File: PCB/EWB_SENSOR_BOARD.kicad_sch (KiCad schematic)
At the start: 31 parts, among them J3 B4B-PH-K-S, J4 Conn_01x06_Pin, U1 ESP32-C3-WROOM-02-N4, U2 AZ1117CD-3.3TRG1, U3 AP64500SP-13, Y1 ABS07-32.768KHZ-T

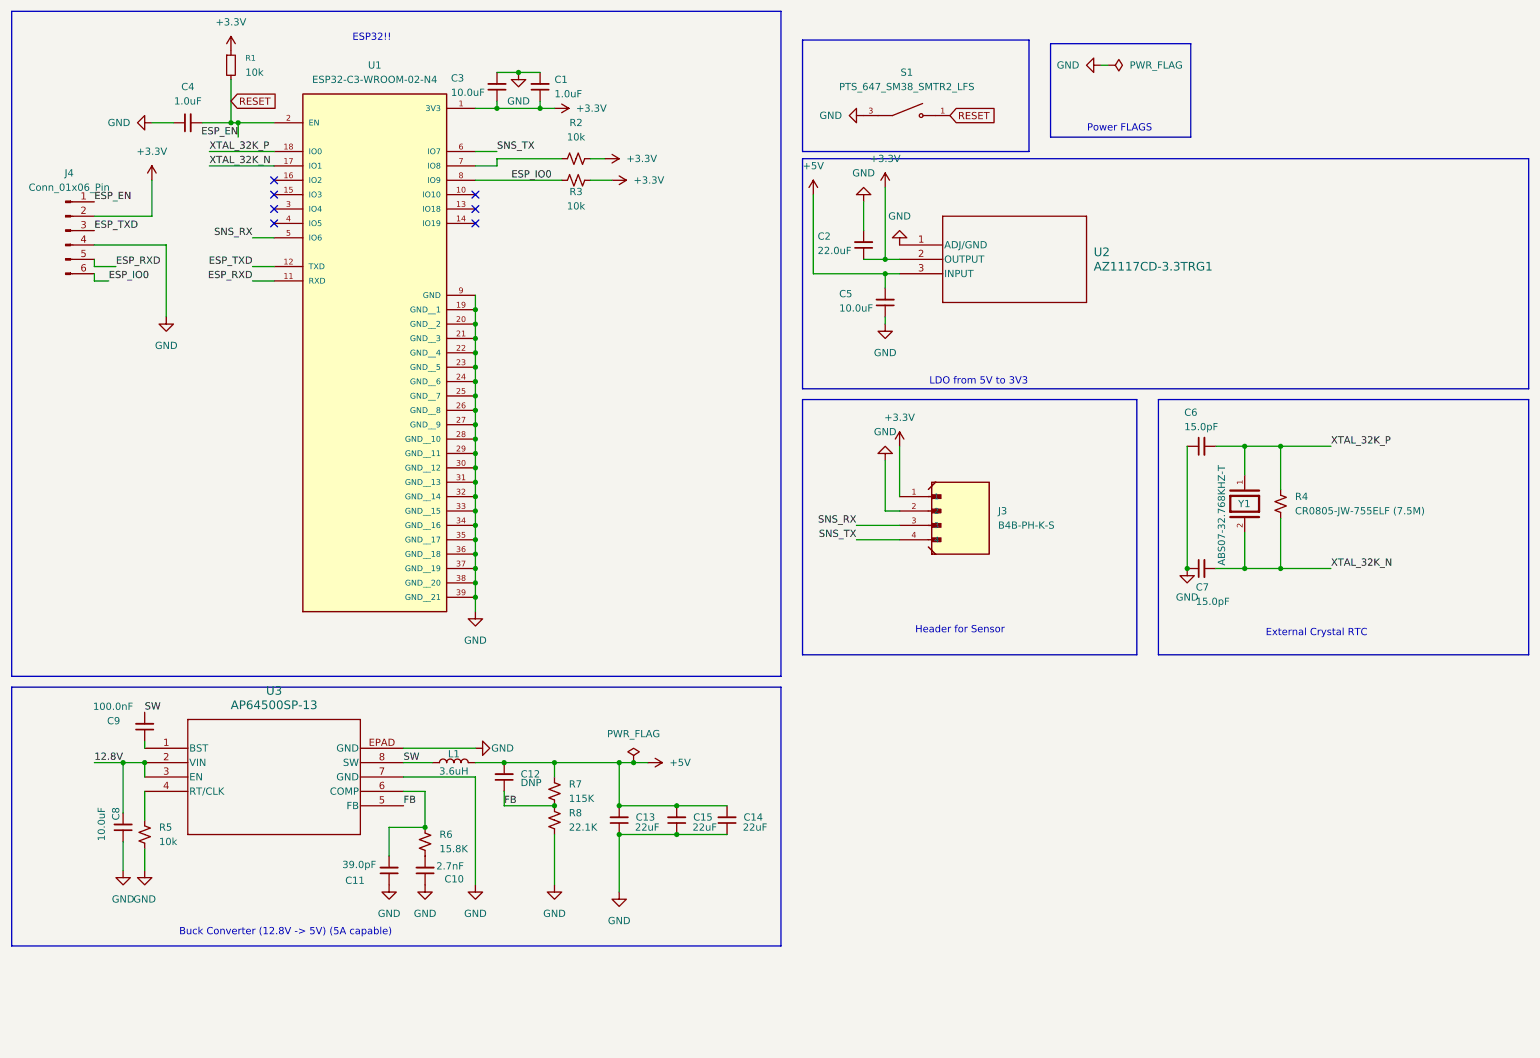
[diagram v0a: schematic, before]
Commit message: Changed LDO to buck, found capacitors and inductors, added bulk capacitance
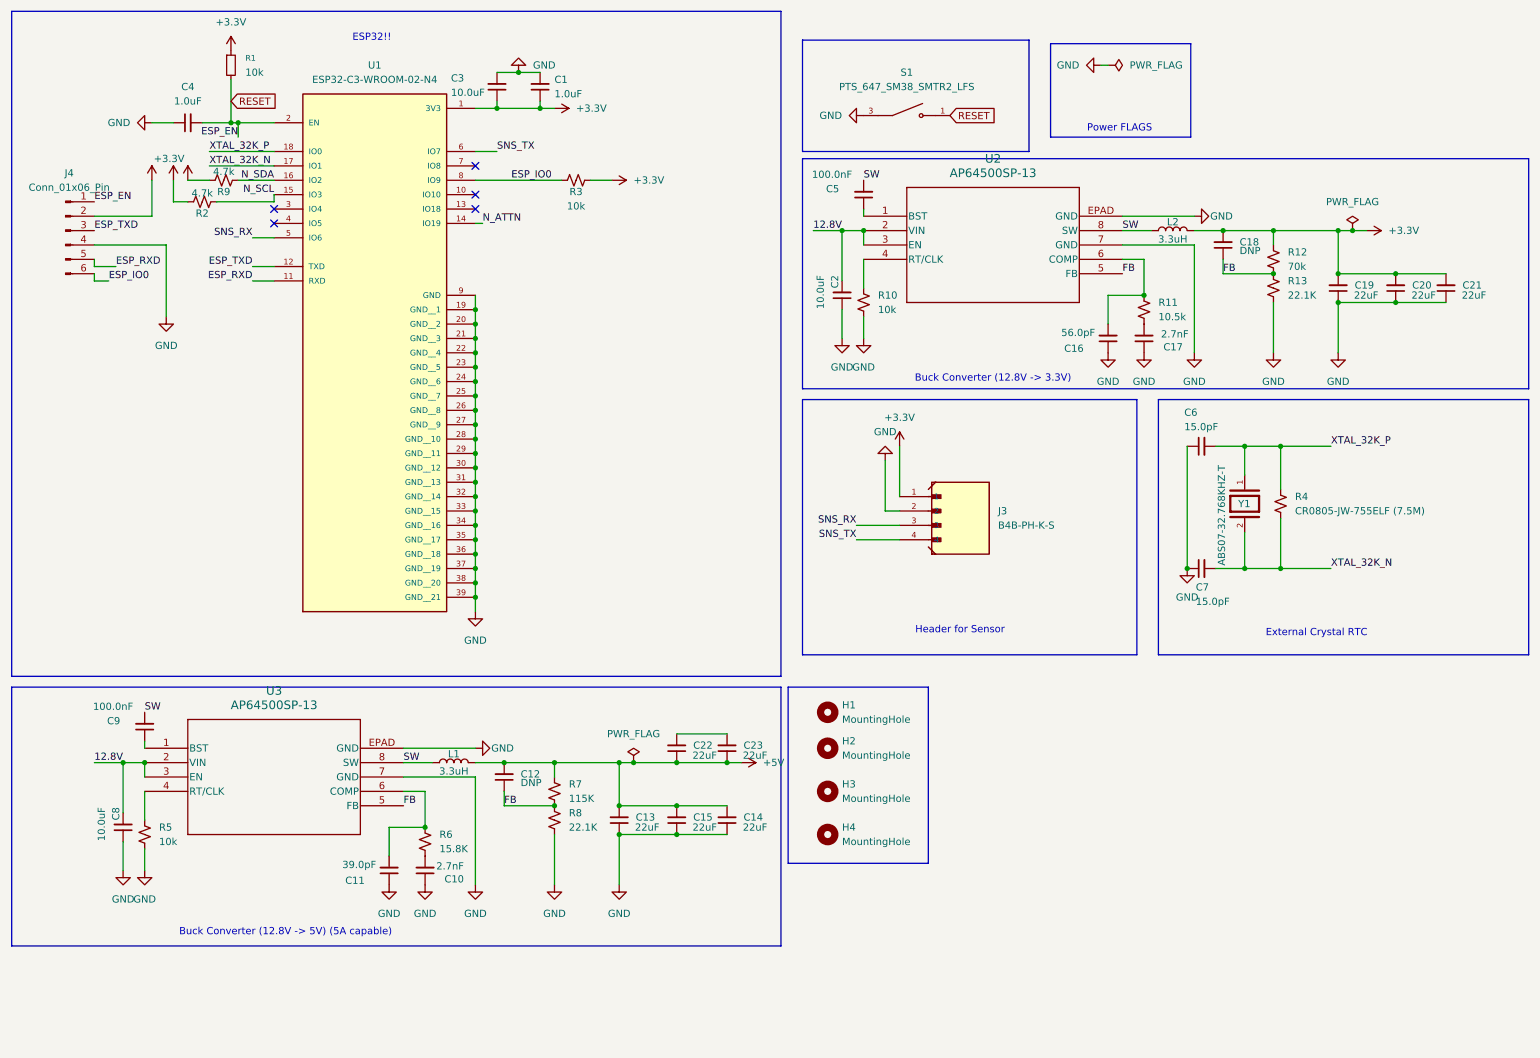
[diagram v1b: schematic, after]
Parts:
- removed U2: AZ1117CD-3.3TRG1, footprints:TO252-2-3.3V_DIO, symbol 2026-02-26_23-08-47:AZ1117CD-3.3TRG1
- added C16: 56.0pF, Capacitor_SMD:C_0805_2012Metric, symbol Device:C_Small
- added C17: 2.7nF, Capacitor_SMD:C_0805_2012Metric, symbol Device:C_Small
- added C18: DNP, Capacitor_SMD:C_0805_2012Metric, symbol Device:C_Small
- added C19, C20, C21, C22, C23: 22uF, CC1210KKX7R8BB226:CAP_CC1210_YAG, symbol Device:C_Small
- added H1, H2, H3, H4: MountingHole, symbol Mechanical:MountingHole
- added L2: 3.3uH, IHLP4040DZER3R3M01:IND_IHLP-4040DZ_VIS, symbol Device:L
- added R10: 10k, Resistor_SMD:R_0805_2012Metric, symbol Device:R_Small_US
- added R11: 10.5k, Resistor_SMD:R_0805_2012Metric, symbol Device:R_Small_US
- added R12: 70k, Resistor_SMD:R_0805_2012Metric, symbol Device:R_Small_US
- added R13: 22.1K, Resistor_SMD:R_0805_2012Metric, symbol Device:R_Small_US
- added R9: 4.7k, Resistor_SMD:R_0805_2012Metric, symbol Device:R_Small_US
- added U2: AP64500SP-13, AP64500SP-13:SO-8EP_DIO, symbol AP64500SP-13:AP64500SP-13
- C13, C14, C15: footprint Capacitor_SMD:C_0805_2012Metric -> CC1210KKX7R8BB226:CAP_CC1210_YAG
- C2: value 22.0uF -> 10.0uF
- C5: value 10.0uF -> 100.0nF
- L1: value 3.6uH -> 3.3uH; footprint Inductor_SMD:L_0805_2012Metric -> IHLP4040DZER3R3M01:IND_IHLP-4040DZ_VIS
- R2: value 10k -> 4.7k
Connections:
- net +3.3V: now also R2.1, C18.2, C19.2, C20.2, C21.2, L2.2, R12.2, R9.1; no longer C2.1, R2.2
- net +5V: now also C22.1, C23.1; no longer C5.2
- net 12.8V: now also C2.2, U2.2 (VIN), U2.3 (EN)
- net FB: now also C18.1, R12.1, R13.2, U2.5 (FB)
- net GND: now also C2.1, C16.1, C17.1, C19.1, C20.1, C21.1, R10.1, R13.1, U2.7 (GND), U2.EPAD (GND); no longer C2.2, C5.1
- net SW: now also C5.2, L2.1, U2.8 (SW)
- net at U1.7 (IO8): no longer R2.1
- net N_ATTN: now reaches U1.14 (IO19)
- net N_SCL: now reaches U1.15 (IO3)
- net N_SCL: now also R2.2
- net N_SDA: now reaches U1.16 (IO2)
- net N_SDA: now also R9.2
- new net: C22.2, C23.2
- new net: C17.2, R11.1
- new net: C16.2, R11.2, U2.6 (COMP)
- new net: C5.1, U2.1 (BST)
- new net: R10.2, U2.4 (RT/CLK)
- no-connect marks 7 -> 5
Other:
- note added: "Buck Converter (12.8V -> 3.3V)"
- note removed: "LDO from 5V to 3V3"

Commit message: almost finished
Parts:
- removed C12, C18: DNP, Capacitor_SMD:C_0805_2012Metric, symbol Device:C_Small
- removed C22, C23: 22uF, CC1210KKX7R8BB226:CAP_CC1210_YAG, symbol Device:C_Small
- removed J4: Conn_01x06_Pin, Connector_PinHeader_2.54mm:PinHeader_1x06_P2.54mm_Vertical, symbol Connector:Conn_01x06_Pin
- added C24: 100uF, EEE_FP1C101AP:CAP_EEEFP1C101AP, symbol Device:C_Small
- added C25: .1uF, Capacitor_SMD:C_0805_2012Metric, symbol Device:C_Small
- added J1, J4: Conn_01x24_Pin, Connector_PinHeader_2.54mm:PinHeader_1x24_P2.54mm_Vertical, symbol Connector:Conn_01x24_Pin
- added J2, J5: Conn_01x03_Pin, Connector_PinSocket_2.54mm:PinSocket_1x03_P2.54mm_Vertical, symbol Connector:Conn_01x03_Pin
- added J6: TB002-500-02BE, TB002_500_02BE:CUI_TB002-500-02BE, symbol TB002-500-02BE:TB002-500-02BE
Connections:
- net +3.3V: now also J2.1 (Pin_1)
- net +5V: now also C24.2, C25.2, J4.7 (Pin_7)
- net 12.8V: now also J6.2
- net ESP_IO0: now also J5.3 (Pin_3)
- net ESP_RXD: now also J5.2 (Pin_2)
- net ESP_TXD: now also J5.1 (Pin_1)
- net FB: no longer R12.1, R13.2, U2.5 (FB)
- net GND: now also C24.1, C25.1, J2.3 (Pin_3), J4.24 (Pin_24), J6.1
- net N_ATTN: now also U1.7 (IO8), J4.14 (Pin_14); no longer U1.14 (IO19)
- net N_SCL: now also J4.12 (Pin_12)
- net N_SDA: now also J4.13 (Pin_13)
- net RESET: now also J2.2 (Pin_2)
- net SNS_RX: now also J3.4; no longer J3.3
- net SNS_TX: now also J3.3; no longer J3.4
- net SW: no longer C5.2, L2.1, U2.8 (SW)
- new net FB_1: R12.1, R13.2, U2.5 (FB)
- new net SW_1: C5.2, L2.1, U2.8 (SW)
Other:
- note added: "Header for 12.8v Battery"
- note added: "Notecarrier Headerpins"

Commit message: Finished PCB?
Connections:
- net N_SCL: now also J1.4 (Pin_4); no longer J4.12 (Pin_12)
- net N_SDA: now also J1.3 (Pin_3); no longer J4.13 (Pin_13)
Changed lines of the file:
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@@
+		)
+	)
+	(label "N_SCL"
+		(at 90.17 185.42 90)
+		(effects
+			(font
+				(size 1.27 1.27)
+			)
+			(justify left bottom)
 		)
 	)
@@
 		)
 	)
-	(label "N_SCL"
-		(at 44.45 185.42 90)
-		(effects
-			(font
-				(size 1.27 1.27)
-			)
-			(justify left bottom)
-		)
-	)
 	(label "SW"
 		(at 36.83 138.43 0)
@@
 	)
 	(label "N_SDA"
-		(at 46.99 185.42 90)
-		(effects
-			(font
+		(at 87.63 185.42 90)
+		(effects
+			(font

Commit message: Final PCB
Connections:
- net N_SCL: now also J4.12 (Pin_12); no longer J1.4 (Pin_4)
- net N_SDA: now also J4.13 (Pin_13); no longer J1.3 (Pin_3)
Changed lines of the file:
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@@
+		)
+	)
+	(label "N_SCL"
+		(at 44.45 185.42 90)
+		(effects
+			(font
+				(size 1.27 1.27)
+			)
+			(justify left bottom)
 		)
 	)
@@
 		)
 	)
-	(label "N_SCL"
-		(at 90.17 185.42 90)
-		(effects
-			(font
-				(size 1.27 1.27)
-			)
-			(justify left bottom)
-		)
-	)
 	(label "ESP_IO0"
 		(at 101.6 44.45 0)
@@
 		)
 	)
+	(label "N_SDA"
+		(at 46.99 185.42 90)
+		(effects
+			(font
+				(size 1.27 1.27)
+			)
+			(justify left bottom)
+		)
+	)
 	(label "N_ATTN"
 		(at 49.53 185.42 90)
@@
 		)
 	)
-	(label "N_SDA"
-		(at 87.63 185.42 90)
-		(effects
-			(font
-				(size 1.27 1.27)
-			)
-			(justify left bottom)
-		)
-	)
